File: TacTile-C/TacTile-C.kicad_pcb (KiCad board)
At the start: 2 copper layers, 59.9 x 59.9 mm, 56 parts, among them J1 Conn_01x02, J10 Conn_01x02, J11 Conn_01x02, J12 Conn_01x02, J13 Conn_01x02, J14 Conn_01x02, J15 Conn_01x02, J16 Conn_01x02, J17 Conn_01x02, J18 Conn_01x06, J19 Conn_01x06, J2 Conn_01x02, J20 Conn_01x06, J21 Conn_01x06, J3 Conn_01x02, J4 Conn_01x02, J5 Conn_01x02, J6 Conn_01x02, J7 Conn_01x02, J8 Conn_01x02, J9 Conn_01x02, U1 74HC4051, U10 74LVC1G18, U11 74LVC2G04, U12 74HC595, U13 74HC590, U14 74LVC2G00, U15 74LVC2G32, U16 74LS74, U17 74LVC1G373, U18 74LVC2G04, U2 74HC4051, U20 74AUC1G74, U3 74HC4051, U4 74HC4051, U5 74HC4051, U6 74LVC2G08, U7 74LVC1G18, U8 74HC4051, U9 74HC4051

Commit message: Began layout and routing of board C
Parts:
- removed U10: 74LVC1G18, Package_DIP:DIP-6_W7.62mm_Socket
- removed U11, U18: 74LVC2G04, Package_DIP:DIP-6_W7.62mm_Socket
- removed U12: 74HC595, Package_DIP:DIP-16_W7.62mm_Socket
- removed U13: 74HC590, Package_DIP:DIP-16_W7.62mm_Socket
- removed U14: 74LVC2G00, Package_DIP:DIP-8_W7.62mm_Socket
- removed U15: 74LVC2G32, Package_DIP:DIP-8_W7.62mm_Socket
- removed U16: 74LS74, Package_DIP:DIP-14_W7.62mm_Socket
- removed U17: 74LVC1G373, Package_DIP:DIP-6_W7.62mm_Socket
- removed U20: 74AUC1G74, Package_DIP:DIP-8_W7.62mm_Socket
- removed U9: 74HC4051, Package_DIP:DIP-16_W7.62mm_Socket
- J18: value Conn_01x06 -> Conn_01x04; footprint Connector_PinHeader_2.00mm:PinHeader_1x06_P2.00mm_Horizontal -> Connector_PinHeader_1.27mm:PinHeader_1x04_P1.27mm_Vertical; moved to B.Cu
- J19: value Conn_01x06 -> Conn_01x05; footprint Connector_PinHeader_2.00mm:PinHeader_1x06_P2.00mm_Horizontal -> Connector_PinHeader_1.27mm:PinHeader_1x05_P1.27mm_Vertical; moved to B.Cu
- J20, J21: value Conn_01x06 -> Conn_01x02; footprint Connector_PinSocket_2.00mm:PinSocket_1x06_P2.00mm_Horizontal -> Connector_PinHeader_1.27mm:PinHeader_1x02_P1.27mm_Vertical; moved to B.Cu
- U1: value 74HC4051 -> 74LVC1G18; footprint Package_DIP:DIP-16_W7.62mm_Socket -> Package_DIP:DIP-6_W7.62mm_Socket
- U6: value 74LVC2G08 -> 74HC4051; footprint Package_DIP:DIP-8_W7.62mm_Socket -> Package_DIP:DIP-16_W7.62mm_Socket
- U7: value 74LVC1G18 -> 74HC4051; footprint Package_DIP:DIP-6_W7.62mm_Socket -> Package_DIP:DIP-16_W7.62mm_Socket
- moved J20 116.8 mm to (35.0, 26.1), turned to -90 degrees
- moved J18 96.7 mm to (35.0, 83.8), turned to -90 degrees
- moved U6 95.7 mm to (34.2, 61.1)
- moved J21 93.2 mm to (73.7, 26.1), turned to -90 degrees
- moved J17 87.6 mm to (25.6, 32.5), turned to 90 degrees
- moved JMP5 86.1 mm to (25.8, 56.2)
- moved JMP6 86.1 mm to (25.8, 58.8)
- moved JMP7 86.0 mm to (25.8, 61.2)
- moved JMP8 86.0 mm to (25.8, 63.8)
- moved JMP1 85.8 mm to (25.8, 46.2)
- moved JMP2 85.7 mm to (25.8, 48.8)
- moved JMP3 85.6 mm to (25.8, 51.2)
- moved JMP4 85.4 mm to (25.8, 53.8)
- moved U7 82.1 mm to (45.5, 61.1)
- moved J5 80.8 mm to (25.6, 40.0), turned to 90 degrees
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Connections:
- J1 pad 1: VIN -> /INP1
- J1 pad 2: GND -> /INP0
- J10 pad 1: /Solenoid_controller/INP17 -> /INP18
- J10 pad 2: /Solenoid_controller/INP16 -> /INP19
- J11 pad 1: /Solenoid_controller/INP18 -> /INP21
- J11 pad 2: /Solenoid_controller/INP19 -> /INP20
- J12 pad 1: /Solenoid_controller/INP21 -> /INP22
- J12 pad 2: /Solenoid_controller/INP20 -> /INP23
- J13 pad 1: /Solenoid_controller/INP22 -> /INP25
- J13 pad 2: /Solenoid_controller/INP23 -> /INP24
- J14 pad 1: /Solenoid_controller/INP25 -> /INP26
- J14 pad 2: /Solenoid_controller/INP24 -> /INP27
- J15 pad 1: /Solenoid_controller/INP26 -> /INP29
- J15 pad 2: /Solenoid_controller/INP27 -> /INP28
- J16 pad 1: /Solenoid_controller/INP29 -> /INP30
- J16 pad 2: /Solenoid_controller/INP28 -> /INP31
- J17 pad 1: /Solenoid_controller/INP30 -> /VIN
- J17 pad 2: /Solenoid_controller/INP31 -> /GND
- J18 pad 1: CLK -> /LS0
- J18 pad 2: MOSI -> /LS1
- J18 pad 3: SS -> /LS2
- J18 pad 4: VIN -> /LS3
- J19 pad 1: CLK -> /LS4
- J19 pad 2: MOSI -> /LS5
- J19 pad 3: SS -> /LS6
- J19 pad 4: VIN -> /LS7
- J19 pad 5: VCC -> /LS8
- J2 pad 1: /Solenoid_controller/INP1 -> /INP2
- J2 pad 2: /Solenoid_controller/INP0 -> /INP3
- J20 pad 1: CLK -> /VIN
- J20 pad 2: MISO0 -> /GND
- J21 pad 1: CLK -> /VCC
- J21 pad 2: MISO1 -> /LEN
- J3 pad 1: /Solenoid_controller/INP2 -> /INP5
- J3 pad 2: /Solenoid_controller/INP3 -> /INP4
- J4 pad 1: /Solenoid_controller/INP5 -> /INP6
- J4 pad 2: /Solenoid_controller/INP4 -> /INP7
- J5 pad 1: /Solenoid_controller/INP6 -> /INP9
- J5 pad 2: /Solenoid_controller/INP7 -> /INP8
- J6 pad 1: /Solenoid_controller/INP9 -> /INP10
- J6 pad 2: /Solenoid_controller/INP8 -> /INP11
- J7 pad 1: /Solenoid_controller/INP10 -> /INP13
- J7 pad 2: /Solenoid_controller/INP11 -> /INP12
- J8 pad 1: /Solenoid_controller/INP13 -> /INP14
- J8 pad 2: /Solenoid_controller/INP12 -> /INP15
- J9 pad 1: /Solenoid_controller/INP14 -> /INP17
- J9 pad 2: /Solenoid_controller/INP15 -> /INP16
- JMP1 pad 1: /Solenoid_controller/INP32 -> /INP32
- JMP10 pad 1: /Solenoid_controller/INP41 -> /INP41
- JMP11 pad 1: /Solenoid_controller/INP42 -> /INP42
- JMP12 pad 1: /Solenoid_controller/INP43 -> /INP43
- JMP13 pad 1: /Solenoid_controller/INP44 -> /INP44
- JMP14 pad 1: /Solenoid_controller/INP45 -> /INP45
- JMP15 pad 1: /Solenoid_controller/INP46 -> /INP46
- JMP16 pad 1: /Solenoid_controller/INP47 -> /INP47
- JMP2 pad 1: /Solenoid_controller/INP33 -> /INP33
- JMP3 pad 1: /Solenoid_controller/INP34 -> /INP34
- JMP4 pad 1: /Solenoid_controller/INP35 -> /INP35
- JMP5 pad 1: /Solenoid_controller/INP36 -> /INP36
- JMP6 pad 1: /Solenoid_controller/INP37 -> /INP37
- JMP7 pad 1: /Solenoid_controller/INP38 -> /INP38
- JMP8 pad 1: /Solenoid_controller/INP39 -> /INP39
- JMP9 pad 1: /Solenoid_controller/INP40 -> /INP40
- U1 pad 1: /Solenoid_controller/INP4 -> /VCC
- U1 pad 2: /Solenoid_controller/INP6 -> /GND
- U1 pad 3: Net-(U1-A) -> /LS5
- U1 pad 4: /Solenoid_controller/INP7 -> Net-(U8-A)
- U1 pad 5: /Solenoid_controller/INP5 -> /VCC
- U1 pad 6: LEN -> Net-(U7-A)
- U2 pad 1: /Solenoid_controller/INP12 -> /INP4
- U2 pad 10: LS1 -> /LS1
- U2 pad 11: LS0 -> /LS0
- U2 pad 12: /Solenoid_controller/INP11 -> /INP3
- U2 pad 13: /Solenoid_controller/INP8 -> /INP0
- U2 pad 14: /Solenoid_controller/INP9 -> /INP1
- U2 pad 15: /Solenoid_controller/INP10 -> /INP2
- U2 pad 16: VCC -> /VCC
- U2 pad 2: /Solenoid_controller/INP14 -> /INP6
- U2 pad 4: /Solenoid_controller/INP15 -> /INP7
- U2 pad 5: /Solenoid_controller/INP13 -> /INP5
- U2 pad 6: LEN -> /LEN
- U2 pad 7: GND -> /GND
- U2 pad 8: GND -> /GND
- U2 pad 9: LS6 -> /LS6
- U3 pad 1: /Solenoid_controller/INP20 -> /INP12
- U3 pad 10: LS1 -> /LS1
- U3 pad 11: LS0 -> /LS0
- U3 pad 12: /Solenoid_controller/INP19 -> /INP11
- U3 pad 13: /Solenoid_controller/INP16 -> /INP8
- U3 pad 14: /Solenoid_controller/INP17 -> /INP9
- U3 pad 15: /Solenoid_controller/INP18 -> /INP10
- U3 pad 16: VCC -> /VCC
- U3 pad 2: /Solenoid_controller/INP22 -> /INP14
- U3 pad 4: /Solenoid_controller/INP23 -> /INP15
- U3 pad 5: /Solenoid_controller/INP21 -> /INP13
- U3 pad 6: LEN -> /LEN
- U3 pad 7: GND -> /GND
- U3 pad 8: GND -> /GND
- U3 pad 9: LS6 -> /LS6
- U4 pad 1: /Solenoid_controller/INP28 -> /INP20
- U4 pad 10: LS1 -> /LS1
- U4 pad 11: LS0 -> /LS0
- U4 pad 12: /Solenoid_controller/INP27 -> /INP19
- U4 pad 13: /Solenoid_controller/INP24 -> /INP16
- U4 pad 14: /Solenoid_controller/INP25 -> /INP17
- U4 pad 15: /Solenoid_controller/INP26 -> /INP18
- U4 pad 16: VCC -> /VCC
- U4 pad 2: /Solenoid_controller/INP30 -> /INP22
- U4 pad 4: /Solenoid_controller/INP31 -> /INP23
- U4 pad 5: /Solenoid_controller/INP29 -> /INP21
- U4 pad 6: LEN -> /LEN
- U4 pad 7: GND -> /GND
- U4 pad 8: GND -> /GND
- U4 pad 9: LS6 -> /LS6
- U5 pad 1: unconnected-(U5-A4-Pad1) -> /INP28
- U5 pad 10: LS8 -> /LS1
- U5 pad 11: LS7 -> /LS0
- U5 pad 12: Net-(U4-A) -> /INP27
- U5 pad 13: Net-(U1-A) -> /INP24
- U5 pad 14: Net-(U2-A) -> /INP25
- U5 pad 15: Net-(U3-A) -> /INP26
- U5 pad 16: VCC -> /VCC
- U5 pad 2: unconnected-(U5-A6-Pad2) -> /INP30
- U5 pad 3: VCC -> Net-(U5-A)
- U5 pad 4: unconnected-(U5-A7-Pad4) -> /INP31
- U5 pad 5: unconnected-(U5-A5-Pad5) -> /INP29
- U5 pad 6: LEN -> /LEN
- U5 pad 7: GND -> /GND
- U5 pad 8: GND -> /GND
- U5 pad 9: GND -> /LS6
- U6 pad 1: Net-(U13-Q0) -> unconnected-(U6-A4-Pad1)
- U6 pad 2: Net-(U13-Q1) -> unconnected-(U6-A6-Pad2)
- U6 pad 3: Net-(U20-C) -> /VCC
- U6 pad 4: GND -> unconnected-(U6-A7-Pad4)
- U6 pad 5: Net-(U16A-~{Q}) -> unconnected-(U6-A5-Pad5)
- U6 pad 6: MOSI -> /LEN
- U6 pad 7: Net-(U12-RCLK) -> /GND
- U6 pad 8: VCC -> /GND
- U7 pad 1: VCC -> /INP36
- U7 pad 2: GND -> /INP38
- U7 pad 3: LS5 -> Net-(U7-A)
- U7 pad 4: Net-(U9-A) -> /INP39
- U7 pad 5: VCC -> /INP37
- U7 pad 6: Net-(U8-A) -> /LEN
- U8 pad 1: /Solenoid_controller/INP36 -> /INP44
- U8 pad 10: LS3 -> /LS3
- U8 pad 11: LS2 -> /LS2
- U8 pad 12: /Solenoid_controller/INP35 -> /INP43
- U8 pad 13: /Solenoid_controller/INP32 -> /INP40
- U8 pad 14: /Solenoid_controller/INP33 -> /INP41
- U8 pad 15: /Solenoid_controller/INP34 -> /INP42
- U8 pad 16: VCC -> /VCC
- U8 pad 2: /Solenoid_controller/INP38 -> /INP46
- U8 pad 4: /Solenoid_controller/INP39 -> /INP47
- U8 pad 5: /Solenoid_controller/INP37 -> /INP45
- U8 pad 6: LEN -> /LEN
- U8 pad 7: GND -> /GND
- U8 pad 8: GND -> /GND
- U8 pad 9: LS4 -> /LS4
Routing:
- net /VCC: track 0.00 -> 121.9 mm
- net /LEN: track 0.00 -> 118.2 mm
- net /INP28: track 0.00 -> 85.3 mm
- net /INP29: track 0.00 -> 84.2 mm, vias 0 -> 1
- net /LS0: track 0.00 -> 79.6 mm, vias 0 -> 2
- net /INP25: track 0.00 -> 77.3 mm, vias 0 -> 1
- net /LS1: track 0.00 -> 76.5 mm, vias 0 -> 1
- net /LS6: track 0.00 -> 74.0 mm
- net /INP24: track 0.00 -> 72.9 mm, vias 0 -> 1
- net /INP20: track 0.00 -> 61.7 mm
- net /INP22: track 0.00 -> 61.1 mm, vias 0 -> 3
- net /INP16: track 0.00 -> 57.5 mm
- net /INP17: track 0.00 -> 56.5 mm
- net /INP30: track 0.00 -> 56.0 mm, vias 0 -> 4
- net /INP23: track 0.00 -> 55.7 mm, vias 0 -> 2
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
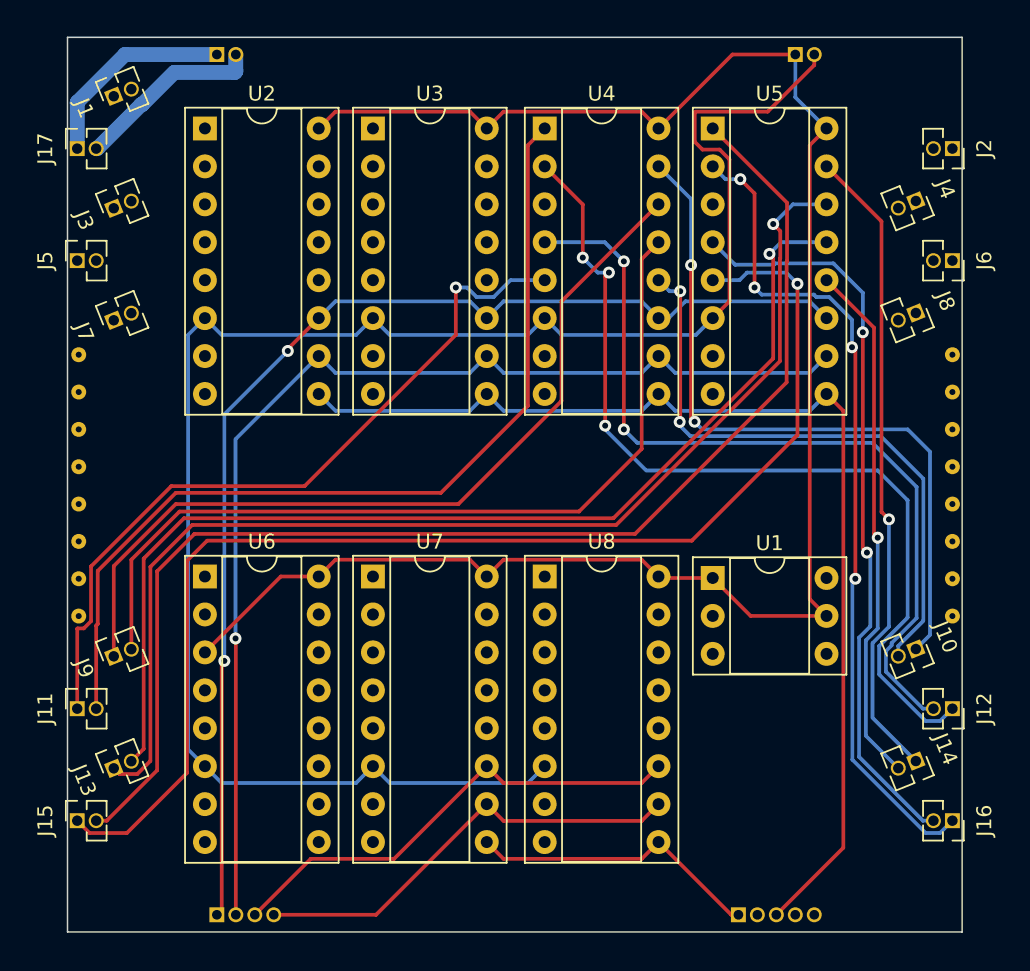
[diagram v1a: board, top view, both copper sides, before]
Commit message: Finished board C layout
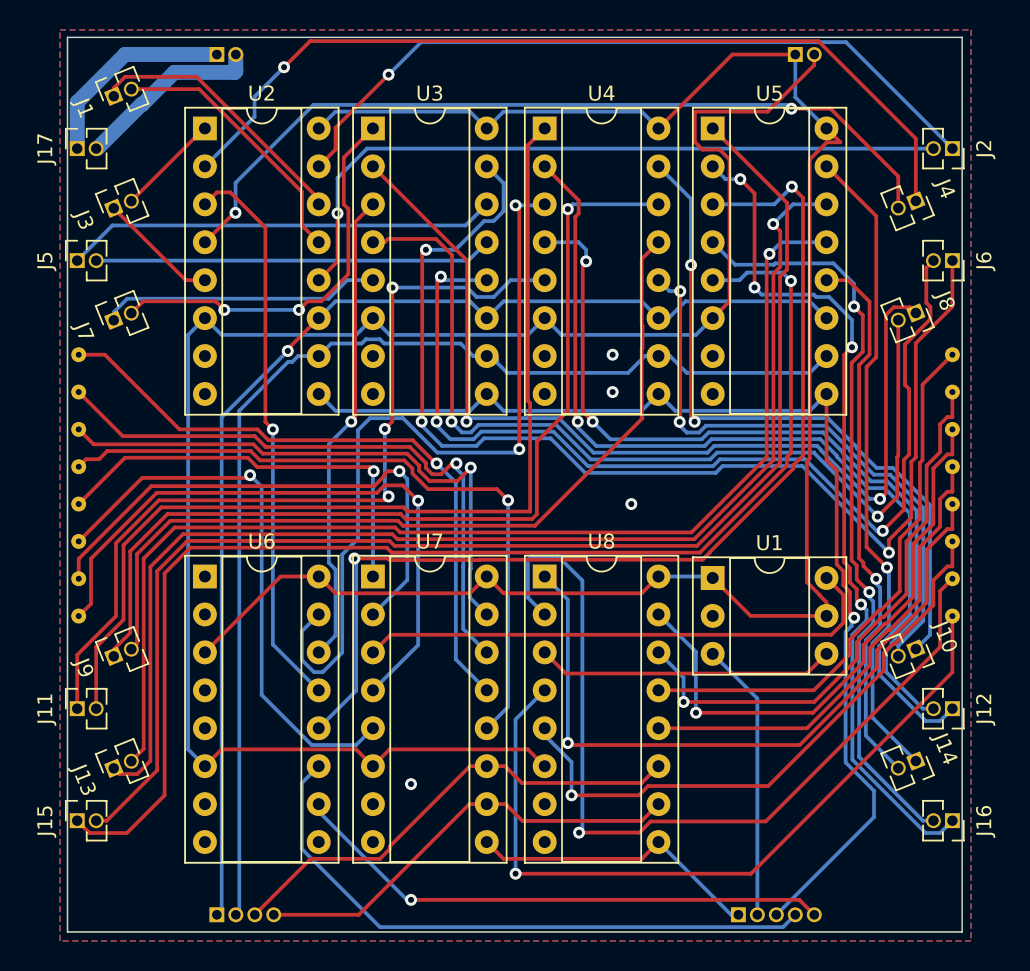
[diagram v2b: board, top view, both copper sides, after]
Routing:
- net /INP10: track 0.00 -> 78.5 mm, vias 0 -> 3
- net Net-(U5-A): track 0.00 -> 69.7 mm, vias 0 -> 2
- net /INP11: track 0.00 -> 66.8 mm, vias 0 -> 3
- net /INP14: track 0.00 -> 65.0 mm, vias 0 -> 2
- net /INP15: track 0.00 -> 62.7 mm, vias 0 -> 2
- net /INP46: track 0.00 -> 59.8 mm, vias 0 -> 1
- net /INP6: track 0.00 -> 58.7 mm, vias 0 -> 1
- net /INP7: track 0.00 -> 55.5 mm, vias 0 -> 2
- net Net-(U4-A): track 0.00 -> 53.0 mm, vias 0 -> 2
- net /INP47: track 0.00 -> 51.7 mm, vias 0 -> 1
- net /INP2: track 0.00 -> 49.7 mm, vias 0 -> 1
- net /INP3: track 0.00 -> 48.1 mm, vias 0 -> 1
- net /INP44: track 0.00 -> 48.0 mm, vias 0 -> 1
- net /INP35: track 0.00 -> 46.6 mm, vias 0 -> 1
- net /INP32: track 0.00 -> 43.7 mm, vias 0 -> 1
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- added copper zone on B.Cu, net /GND
- added copper zone on F.Cu, net /GND

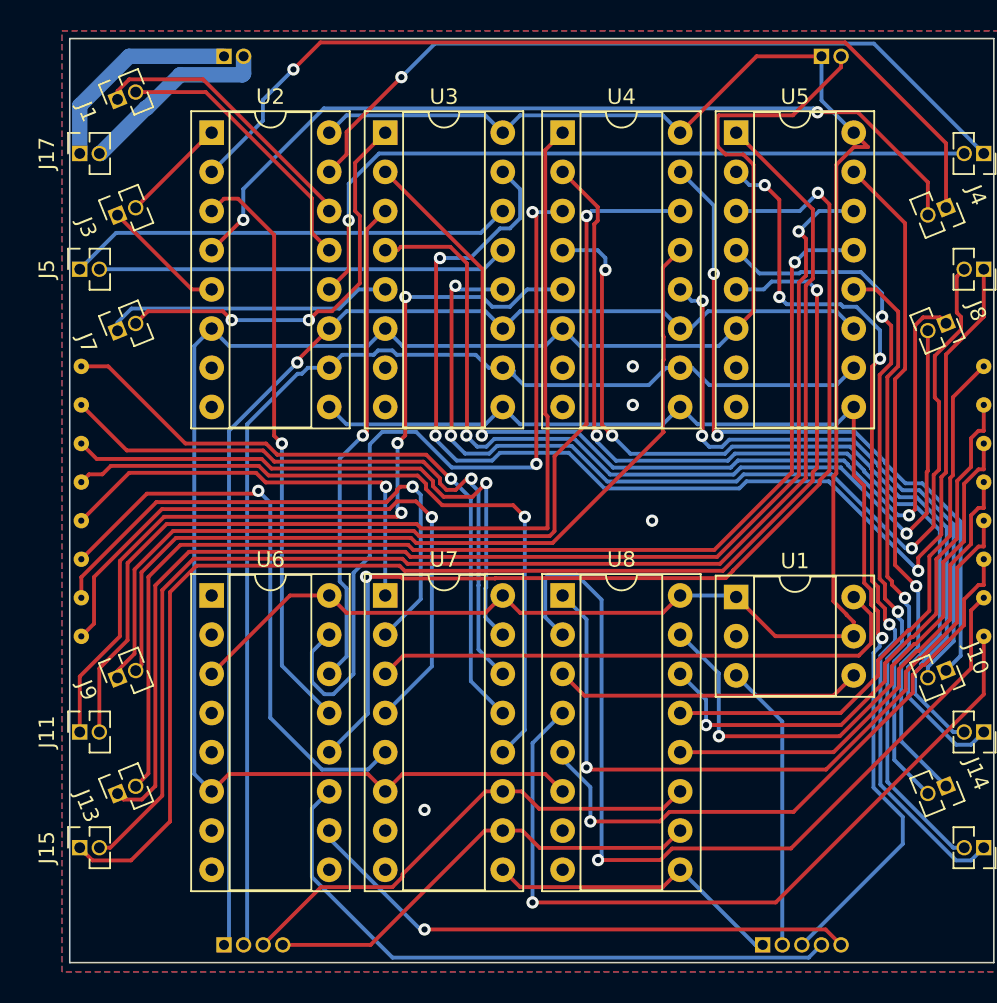
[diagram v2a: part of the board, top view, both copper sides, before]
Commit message: Selected and placed footprints for board D
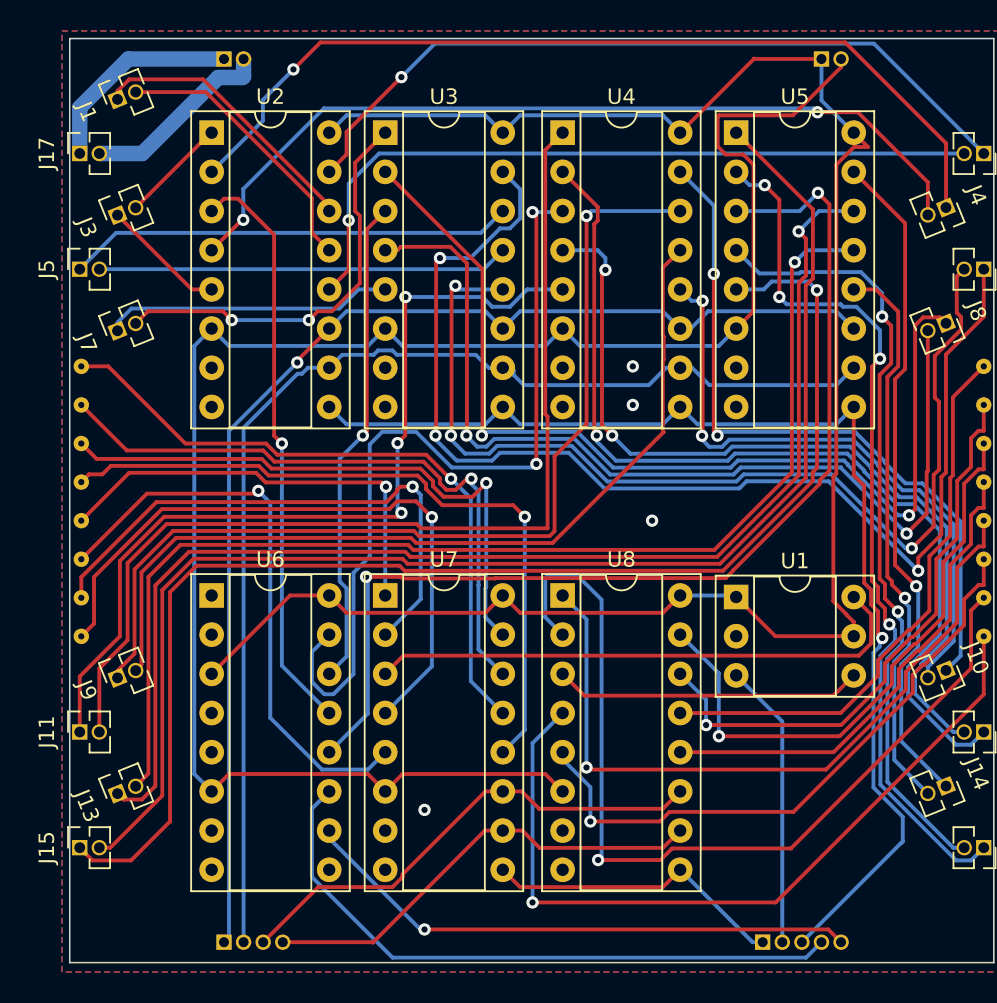
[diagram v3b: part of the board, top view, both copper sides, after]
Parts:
- moved J20 0.18 mm to (35.0, 26.3)
- moved J21 0.18 mm to (73.7, 26.3)
- moved J18 0.17 mm to (35.0, 83.6)
- moved J19 0.17 mm to (69.9, 83.6)
